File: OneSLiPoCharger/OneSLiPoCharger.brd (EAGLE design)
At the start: 86.4 x 52.1 mm, 58 parts, among them IC1 LM358N, Q1 BUZ10

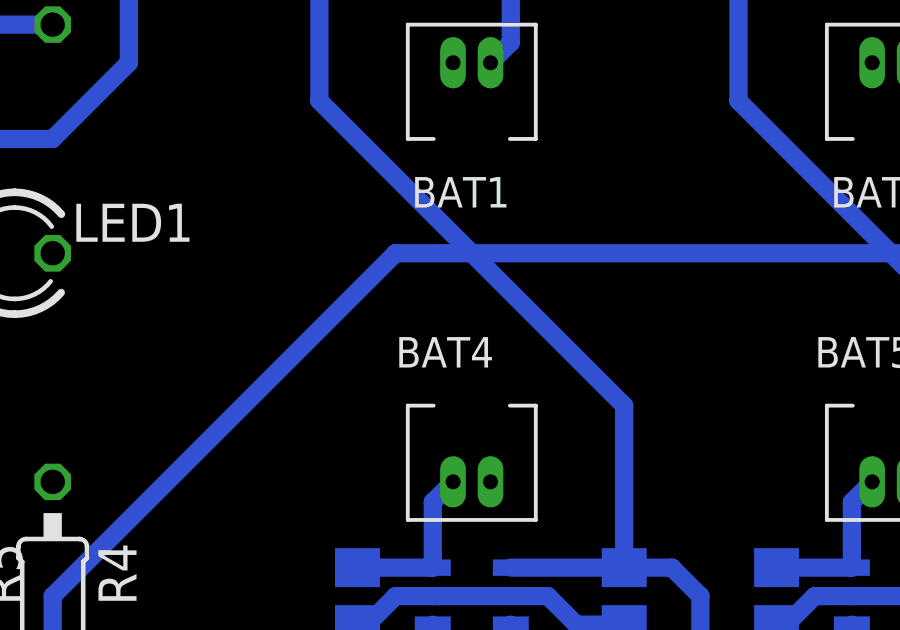
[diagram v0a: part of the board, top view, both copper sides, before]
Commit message: Clean up addition of the buck module.
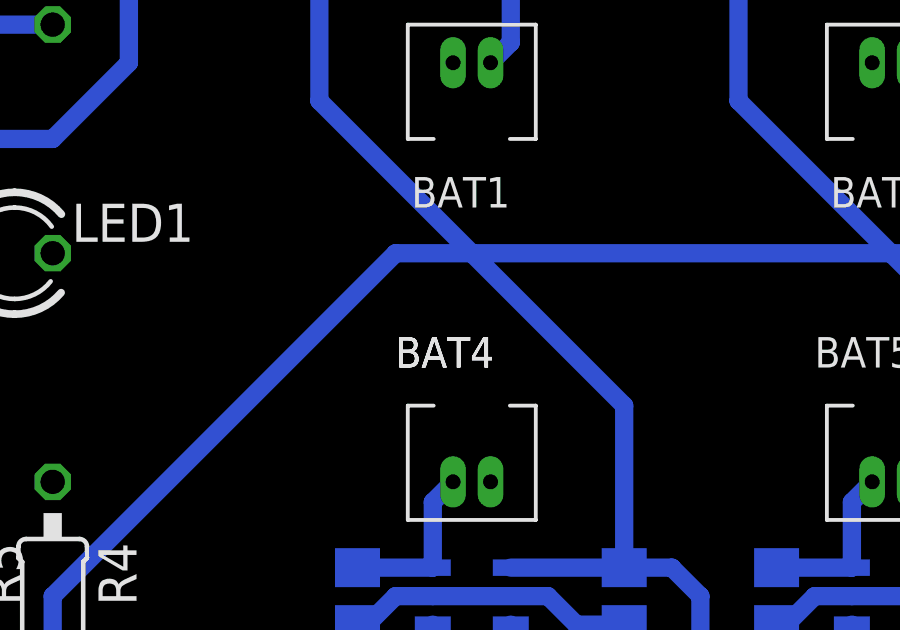
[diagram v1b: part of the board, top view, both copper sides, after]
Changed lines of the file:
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@@
 <grid distance="0.05" unitdist="inch" unit="inch" style="lines" multiple="1" display="no" altdistance="0.025" altunitdist="inch" altunit="inch"/>
 <layers>
-<layer number="1" name="Top" color="4" fill="1" visible="no" active="yes"/>
-<layer number="16" name="Bottom" color="1" fill="1" visible="no" active="yes"/>
-<layer number="17" name="Pads" color="2" fill="1" visible="no" active="yes"/>
-<layer number="18" name="Vias" color="2" fill="1" visible="no" active="yes"/>
-<layer number="19" name="Unrouted" color="6" fill="1" visible="no" active="yes"/>
+<layer number="1" name="Top" color="4" fill="1" visible="yes" active="yes"/>
+<layer number="16" name="Bottom" color="1" fill="1" visible="yes" active="yes"/>
+<layer number="17" name="Pads" color="2" fill="1" visible="yes" active="yes"/>
+<layer number="18" name="Vias" color="2" fill="1" visible="yes" active="yes"/>
+<layer number="19" name="Unrouted" color="6" fill="1" visible="yes" active="yes"/>
 <layer number="20" name="Dimension" color="15" fill="1" visible="yes" active="yes"/>
-<layer number="21" name="tPlace" color="7" fill="1" visible="no" active="yes"/>
-<layer number="22" name="bPlace" color="7" fill="1" visible="no" active="yes"/>
-<layer number="23" name="tOrigins" color="15" fill="1" visible="no" active="yes"/>
-<layer number="24" name="bOrigins" color="15" fill="1" visible="no" active="yes"/>
+<layer number="21" name="tPlace" color="7" fill="1" visible="yes" active="yes"/>
+<layer number="22" name="bPlace" color="7" fill="1" visible="yes" active="yes"/>
+<layer number="23" name="tOrigins" color="15" fill="1" visible="yes" active="yes"/>
+<layer number="24" name="bOrigins" color="15" fill="1" visible="yes" active="yes"/>
 <layer number="25" name="tNames" color="7" fill="1" visible="no" active="yes"/>
 <layer number="26" name="bNames" color="7" fill="1" visible="no" active="yes"/>
@@
 <layer number="28" name="bValues" color="7" fill="1" visible="no" active="yes"/>
 <layer number="29" name="tStop" color="7" fill="3" visible="no" active="yes"/>
-<layer number="30" name="bStop" color="11" fill="1" visible="yes" active="yes"/>
+<layer number="30" name="bStop" color="11" fill="1" visible="no" active="yes"/>
 <layer number="31" name="tCream" color="7" fill="4" visible="no" active="yes"/>
 <layer number="32" name="bCream" color="7" fill="5" visible="no" active="yes"/>
@@
 <wire x1="23.368" y1="24.384" x2="22.352" y2="23.368" width="0.1016" layer="146"/>
 <wire x1="22.352" y1="23.368" x2="22.352" y2="24.384" width="0.1016" layer="146"/>
+<text x="45.72" y="22.86" size="1.016" layer="21">BAT4</text>
 </plain>
 <attributes>
@@
 <wire x1="48.26" y1="26.67" x2="62.23" y2="26.67" width="0.6096" layer="16"/>
 <wire x1="53.34" y1="21.59" x2="48.26" y2="26.67" width="0.6096" layer="16"/>
-<wire x1="45.72" y1="26.67" x2="48.26" y2="26.67" width="0.6096" layer="16"/>
+<wire x1="48.26" y1="26.67" x2="45.72" y2="26.67" width="0.6096" layer="16"/>
 <contactref element="JP1" pad="1"/>
 <contactref element="IC1" pad="6"/>
